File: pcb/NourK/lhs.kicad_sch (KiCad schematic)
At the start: 1 part, among them J1 SJ-435107RS

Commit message: Draft LHS tracks
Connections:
- net GND: now also J1.SH1, J1.SH2
- net USART_RX renamed USART.TX
- net USART_TX renamed USART.RX
- no-connect marks 2 -> 3
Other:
- removed sheet STM32L082 Setup
- added sheet LHS Core (core.kicad_sch)
- sheet LHS Keys ports: added KEY{ROW[1..10] COL[1..10]}; removed KEY_COL1, KEY_COL2, KEY_COL3, KEY_COL4, KEY_COL5, KEY_COL6, KEY_COL7, KEY_ROW1, KEY_ROW2, KEY_ROW3, KEY_ROW4
- sheet LHS LEDs ports: added LED{CS_COL[1..16]}, LED{SW_RED[1..4] SW_GREEN[1..4] SW_BLUE[1..4]}; removed SCL, SDA
- note added: "B2B connector"
- note removed: "Side connector"

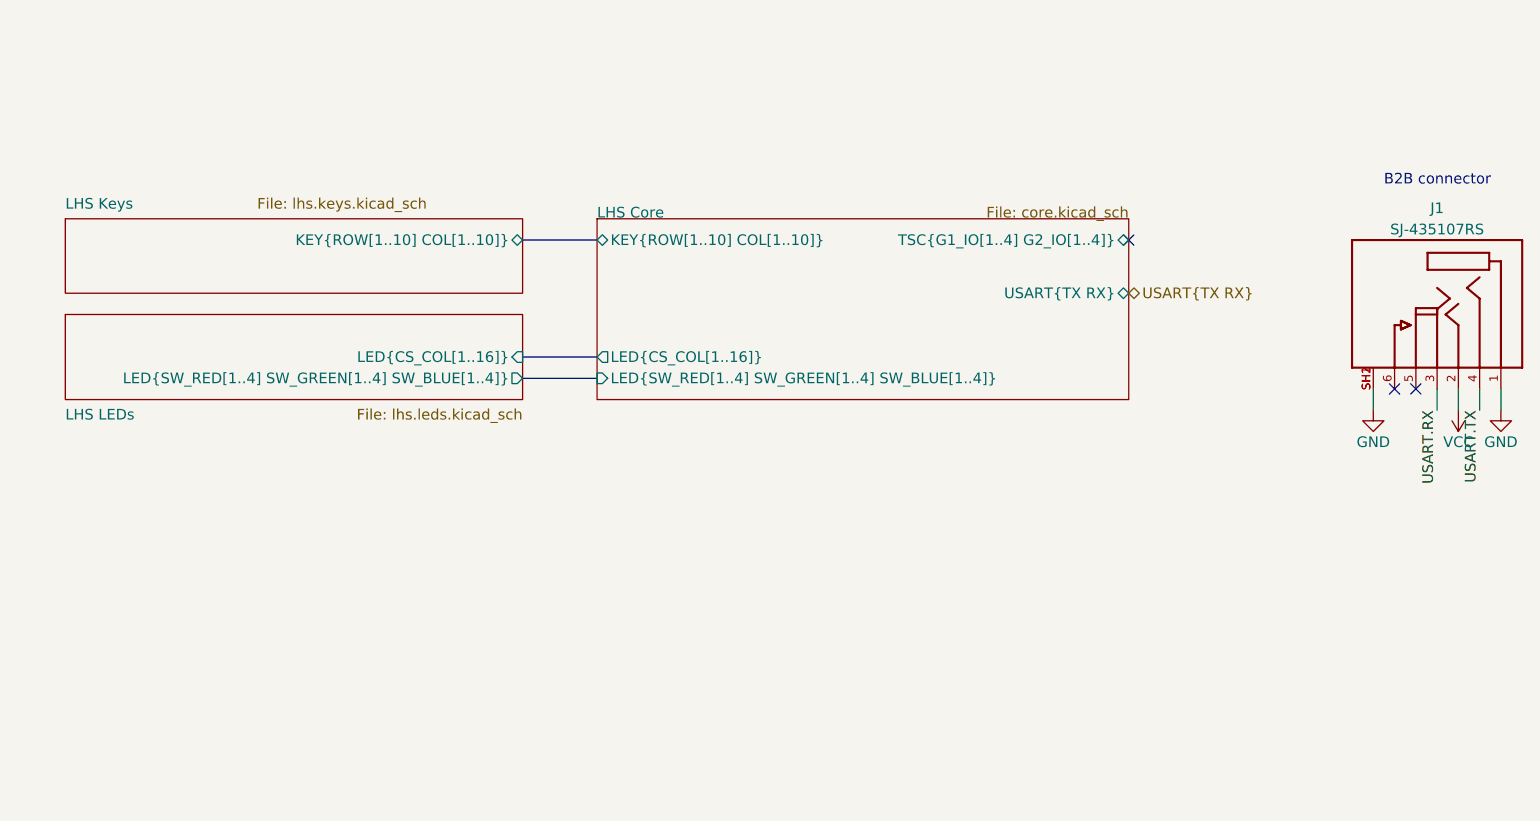
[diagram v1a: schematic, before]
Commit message: Re-traced RHS
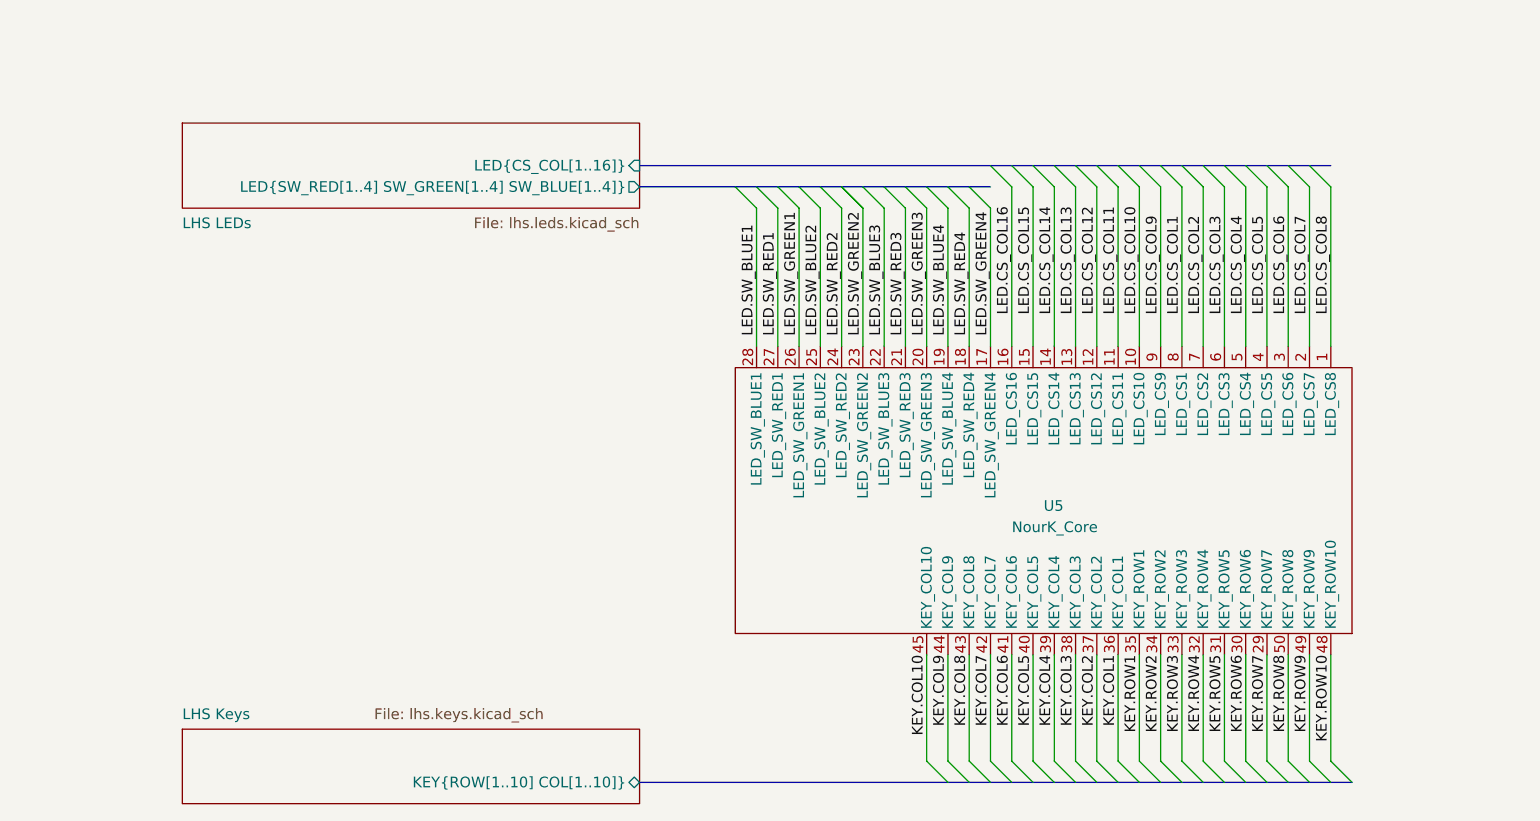
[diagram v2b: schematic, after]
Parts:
- removed J1: SJ-435107RS, Nour_KB:CUI_SJ-435107RS, symbol Nour_KB:SJ-435107RS
- added U5: NourK_Core, Nour_KB:NourKB_Core, symbol Nour_KB:NourK_Core
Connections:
- new net KEY.COL1: U5.36 (KEY_COL1)
- new net KEY.COL10: U5.45 (KEY_COL10)
- new net KEY.COL2: U5.37 (KEY_COL2)
- new net KEY.COL3: U5.38 (KEY_COL3)
- new net KEY.COL4: U5.39 (KEY_COL4)
- new net KEY.COL5: U5.40 (KEY_COL5)
- new net KEY.COL6: U5.41 (KEY_COL6)
- new net KEY.COL7: U5.42 (KEY_COL7)
- new net KEY.COL8: U5.43 (KEY_COL8)
- new net KEY.COL9: U5.44 (KEY_COL9)
- new net KEY.ROW1: U5.35 (KEY_ROW1)
- new net KEY.ROW10: U5.48 (KEY_ROW10)
- new net KEY.ROW2: U5.34 (KEY_ROW2)
- new net KEY.ROW3: U5.33 (KEY_ROW3)
- new net KEY.ROW4: U5.32 (KEY_ROW4)
- new net KEY.ROW5: U5.31 (KEY_ROW5)
- new net KEY.ROW6: U5.30 (KEY_ROW6)
- new net KEY.ROW7: U5.29 (KEY_ROW7)
- new net KEY.ROW8: U5.50 (KEY_ROW8)
- new net KEY.ROW9: U5.49 (KEY_ROW9)
- new net LED.CS_COL1: U5.8 (LED_CS1)
- new net LED.CS_COL10: U5.10 (LED_CS10)
- new net LED.CS_COL11: U5.11 (LED_CS11)
- new net LED.CS_COL12: U5.12 (LED_CS12)
- new net LED.CS_COL13: U5.13 (LED_CS13)
- new net LED.CS_COL14: U5.14 (LED_CS14)
- new net LED.CS_COL15: U5.15 (LED_CS15)
- new net LED.CS_COL16: U5.16 (LED_CS16)
- new net LED.CS_COL2: U5.7 (LED_CS2)
- new net LED.CS_COL3: U5.6 (LED_CS3)
- new net LED.CS_COL4: U5.5 (LED_CS4)
- new net LED.CS_COL5: U5.4 (LED_CS5)
- new net LED.CS_COL6: U5.3 (LED_CS6)
- new net LED.CS_COL7: U5.2 (LED_CS7)
- new net LED.CS_COL8: U5.1 (LED_CS8)
- new net LED.CS_COL9: U5.9 (LED_CS9)
- new net LED.SW_BLUE1: U5.28 (LED_SW_BLUE1)
- new net LED.SW_BLUE2: U5.25 (LED_SW_BLUE2)
- new net LED.SW_BLUE3: U5.22 (LED_SW_BLUE3)
- new net LED.SW_BLUE4: U5.19 (LED_SW_BLUE4)
- new net LED.SW_GREEN1: U5.26 (LED_SW_GREEN1)
- new net LED.SW_GREEN2: U5.23 (LED_SW_GREEN2)
- new net LED.SW_GREEN3: U5.20 (LED_SW_GREEN3)
- new net LED.SW_GREEN4: U5.17 (LED_SW_GREEN4)
- new net LED.SW_RED1: U5.27 (LED_SW_RED1)
- new net LED.SW_RED2: U5.24 (LED_SW_RED2)
- new net LED.SW_RED3: U5.21 (LED_SW_RED3)
- new net LED.SW_RED4: U5.18 (LED_SW_RED4)
- no-connect marks 3 -> 0
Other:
- removed sheet LHS Core
- note removed: "B2B connector"

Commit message: RHS and LHS wire complete and initial DRC
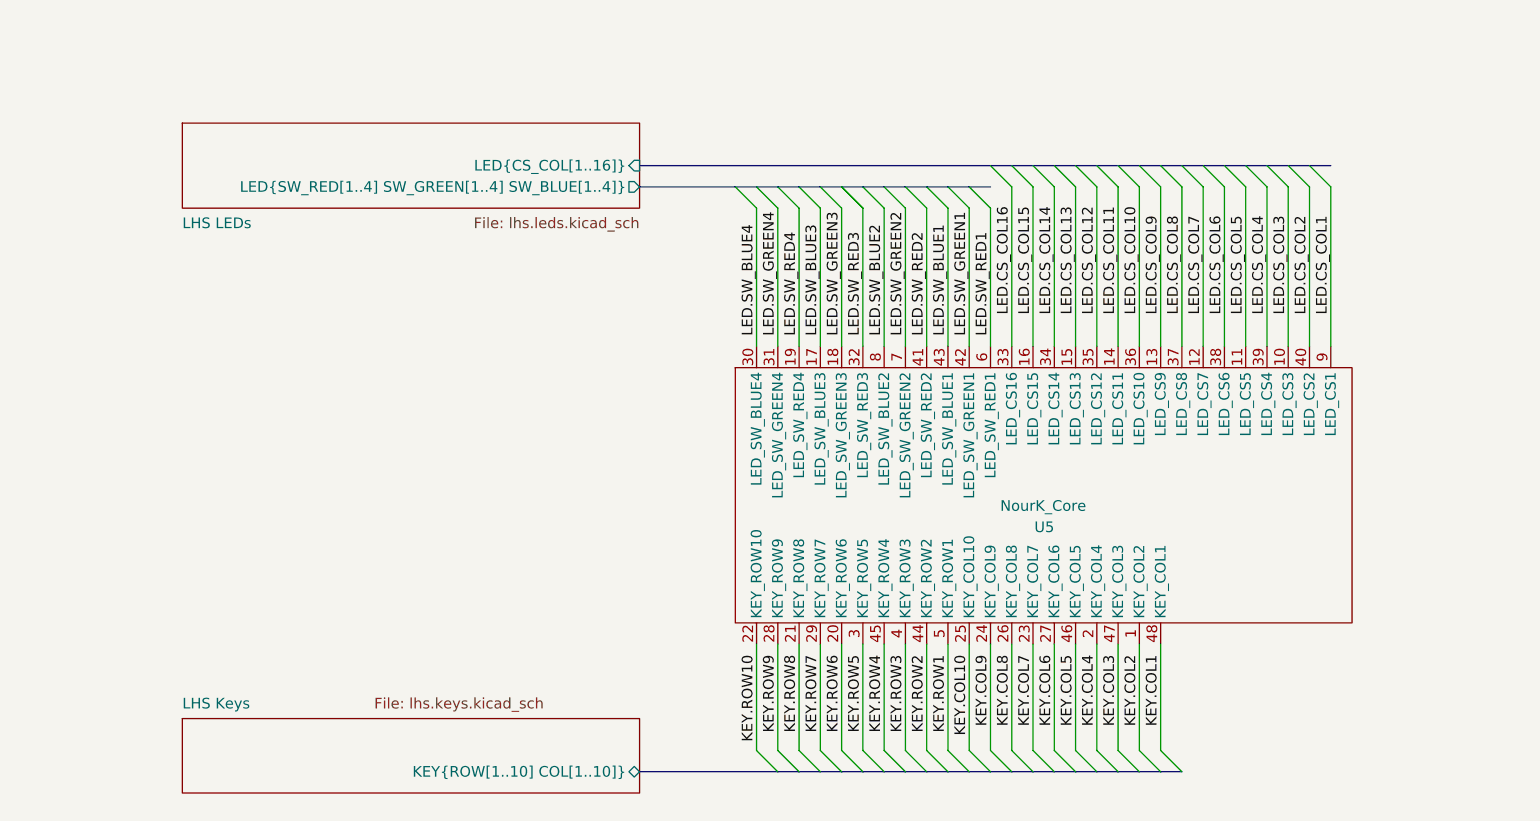
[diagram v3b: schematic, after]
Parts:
- U5: footprint Nour_KB:NourKB_Core -> Nour_KB:NourKB_Core_2; symbol Nour_KB:NourK_Core -> Nour_KB:NourK_Core_3
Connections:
- net KEY.COL1: now also U5.48 (KEY_COL1); no longer U5.36 (KEY_COL1)
- net KEY.COL10: now also U5.25 (KEY_COL10); no longer U5.45 (KEY_COL10)
- net KEY.COL2: now also U5.1 (KEY_COL2); no longer U5.37 (KEY_COL2)
- net KEY.COL3: now also U5.47 (KEY_COL3); no longer U5.38 (KEY_COL3)
- net KEY.COL4: now also U5.2 (KEY_COL4); no longer U5.39 (KEY_COL4)
- net KEY.COL5: now also U5.46 (KEY_COL5); no longer U5.40 (KEY_COL5)
- net KEY.COL6: now also U5.27 (KEY_COL6); no longer U5.41 (KEY_COL6)
- net KEY.COL7: now also U5.23 (KEY_COL7); no longer U5.42 (KEY_COL7)
- net KEY.COL8: now also U5.26 (KEY_COL8); no longer U5.43 (KEY_COL8)
- net KEY.COL9: now also U5.24 (KEY_COL9); no longer U5.44 (KEY_COL9)
- net KEY.ROW1: now also U5.5 (KEY_ROW1); no longer U5.35 (KEY_ROW1)
- net KEY.ROW10: now also U5.22 (KEY_ROW10); no longer U5.48 (KEY_ROW10)
- net KEY.ROW2: now also U5.44 (KEY_ROW2); no longer U5.34 (KEY_ROW2)
- net KEY.ROW3: now also U5.4 (KEY_ROW3); no longer U5.33 (KEY_ROW3)
- net KEY.ROW4: now also U5.45 (KEY_ROW4); no longer U5.32 (KEY_ROW4)
- net KEY.ROW5: now also U5.3 (KEY_ROW5); no longer U5.31 (KEY_ROW5)
- net KEY.ROW6: now also U5.20 (KEY_ROW6); no longer U5.30 (KEY_ROW6)
- net KEY.ROW8: now also U5.21 (KEY_ROW8); no longer U5.50 (KEY_ROW8)
- net KEY.ROW9: now also U5.28 (KEY_ROW9); no longer U5.49 (KEY_ROW9)
- net LED.CS_COL1: now also U5.9 (LED_CS1); no longer U5.8 (LED_CS1)
- net LED.CS_COL10: now also U5.36 (LED_CS10); no longer U5.10 (LED_CS10)
- net LED.CS_COL11: now also U5.14 (LED_CS11); no longer U5.11 (LED_CS11)
- net LED.CS_COL12: now also U5.35 (LED_CS12); no longer U5.12 (LED_CS12)
- net LED.CS_COL13: now also U5.15 (LED_CS13); no longer U5.13 (LED_CS13)
- net LED.CS_COL14: now also U5.34 (LED_CS14); no longer U5.14 (LED_CS14)
- net LED.CS_COL15: now also U5.16 (LED_CS15); no longer U5.15 (LED_CS15)
- net LED.CS_COL16: now also U5.33 (LED_CS16); no longer U5.16 (LED_CS16)
- net LED.CS_COL2: now also U5.40 (LED_CS2); no longer U5.7 (LED_CS2)
- net LED.CS_COL3: now also U5.10 (LED_CS3); no longer U5.6 (LED_CS3)
- net LED.CS_COL4: now also U5.39 (LED_CS4); no longer U5.5 (LED_CS4)
- net LED.CS_COL5: now also U5.11 (LED_CS5); no longer U5.4 (LED_CS5)
- net LED.CS_COL6: now also U5.38 (LED_CS6); no longer U5.3 (LED_CS6)
- net LED.CS_COL7: now also U5.12 (LED_CS7); no longer U5.2 (LED_CS7)
- net LED.CS_COL8: now also U5.37 (LED_CS8); no longer U5.1 (LED_CS8)
- net LED.CS_COL9: now also U5.13 (LED_CS9); no longer U5.9 (LED_CS9)
- net LED.SW_BLUE1: now also U5.43 (LED_SW_BLUE1); no longer U5.28 (LED_SW_BLUE1)
- net LED.SW_BLUE2: now also U5.8 (LED_SW_BLUE2); no longer U5.25 (LED_SW_BLUE2)
- net LED.SW_BLUE3: now also U5.17 (LED_SW_BLUE3); no longer U5.22 (LED_SW_BLUE3)
- net LED.SW_BLUE4: now also U5.30 (LED_SW_BLUE4); no longer U5.19 (LED_SW_BLUE4)
- net LED.SW_GREEN1: now also U5.42 (LED_SW_GREEN1); no longer U5.26 (LED_SW_GREEN1)
- net LED.SW_GREEN2: now also U5.7 (LED_SW_GREEN2); no longer U5.23 (LED_SW_GREEN2)
- net LED.SW_GREEN3: now also U5.18 (LED_SW_GREEN3); no longer U5.20 (LED_SW_GREEN3)
- net LED.SW_GREEN4: now also U5.31 (LED_SW_GREEN4); no longer U5.17 (LED_SW_GREEN4)
- net LED.SW_RED1: now also U5.6 (LED_SW_RED1); no longer U5.27 (LED_SW_RED1)
- net LED.SW_RED2: now also U5.41 (LED_SW_RED2); no longer U5.24 (LED_SW_RED2)
- net LED.SW_RED3: now also U5.32 (LED_SW_RED3); no longer U5.21 (LED_SW_RED3)
- net LED.SW_RED4: now also U5.19 (LED_SW_RED4); no longer U5.18 (LED_SW_RED4)
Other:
- moved on the sheet: U5
